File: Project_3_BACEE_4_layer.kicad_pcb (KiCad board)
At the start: 2 copper layers, 42.2 x 27.4 mm, 17 parts, among them J1 Digital pins, J2 Serial, J3 ICSP, J4 I2C, U1 24LC1025, U2 24LC1025, U3 DS1337S+, U4 ATMEGA328P-AU, Y1 Crystal 32 MHz, Y2 Crystal 16 MHz

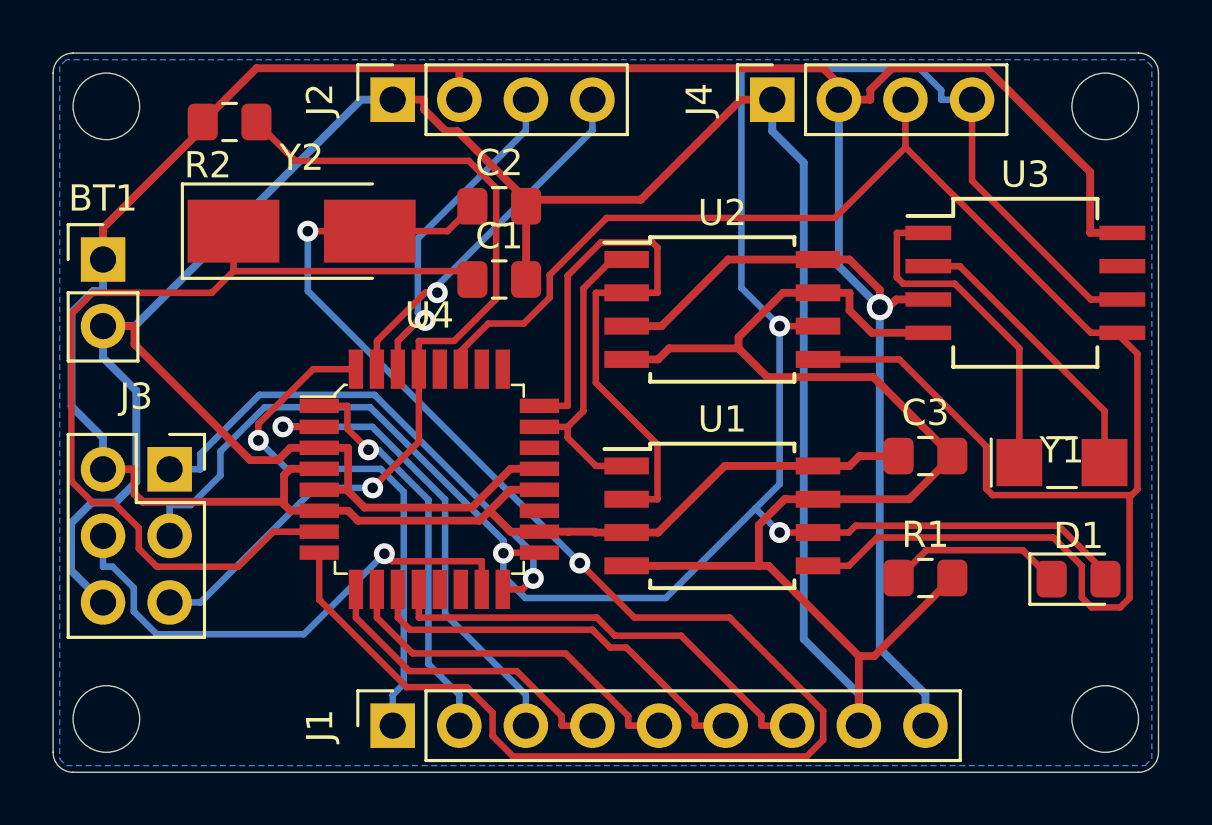
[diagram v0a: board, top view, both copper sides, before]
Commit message: Created copper filled area for 2 layer board.
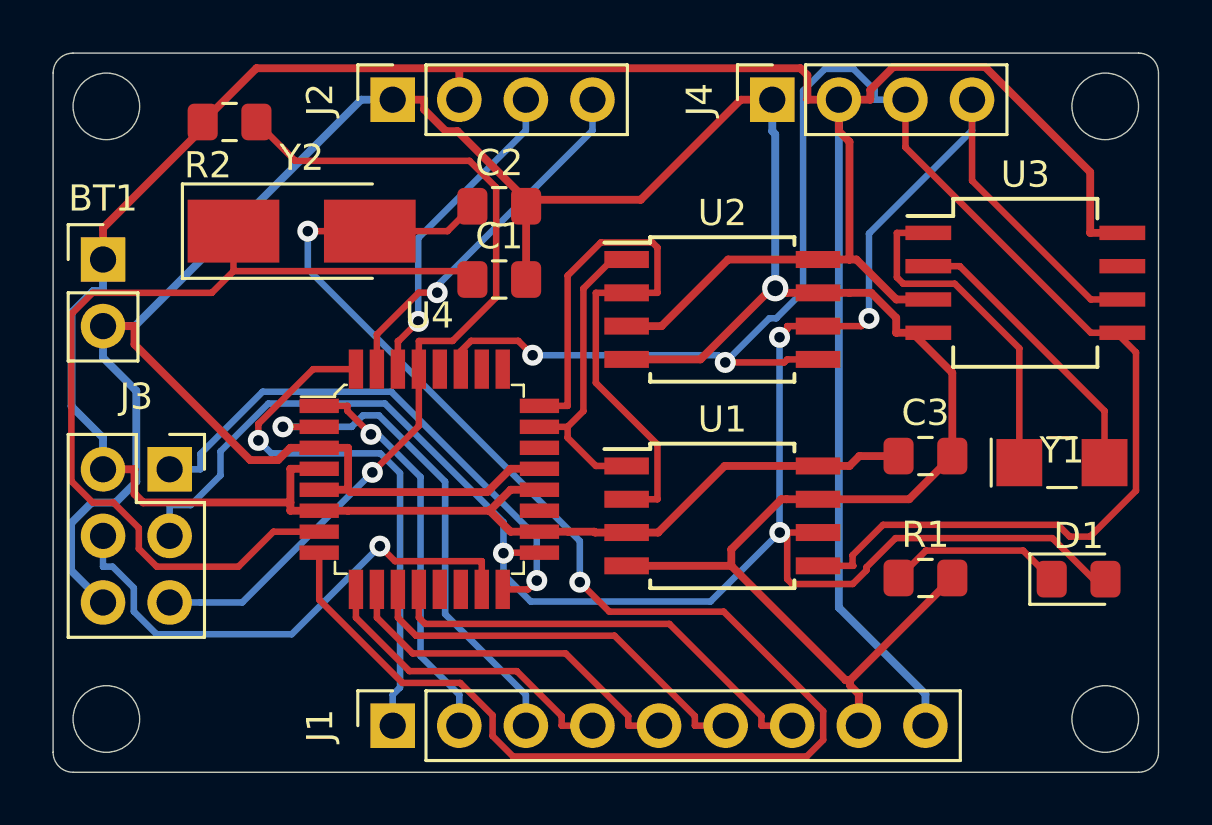
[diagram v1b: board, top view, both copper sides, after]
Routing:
- net GNDPWR: track 148.3 -> 125.6 mm, vias 0 -> 1
- net /SDA: track 74.3 -> 64.9 mm, vias 0 -> 2
- net /Vcc: track 136.2 -> 141.5 mm, vias 1 -> 0
- net /SCK: track 86.4 -> 82.2 mm, vias 3 -> 4
- net /MISO: track 20.2 -> 21.0 mm
- net /D4: track 18.6 -> 19.4 mm
- removed copper zone on B.Cu, net GNDPWR
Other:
- copper layers 2 -> 4
